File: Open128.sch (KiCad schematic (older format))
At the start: 0 parts

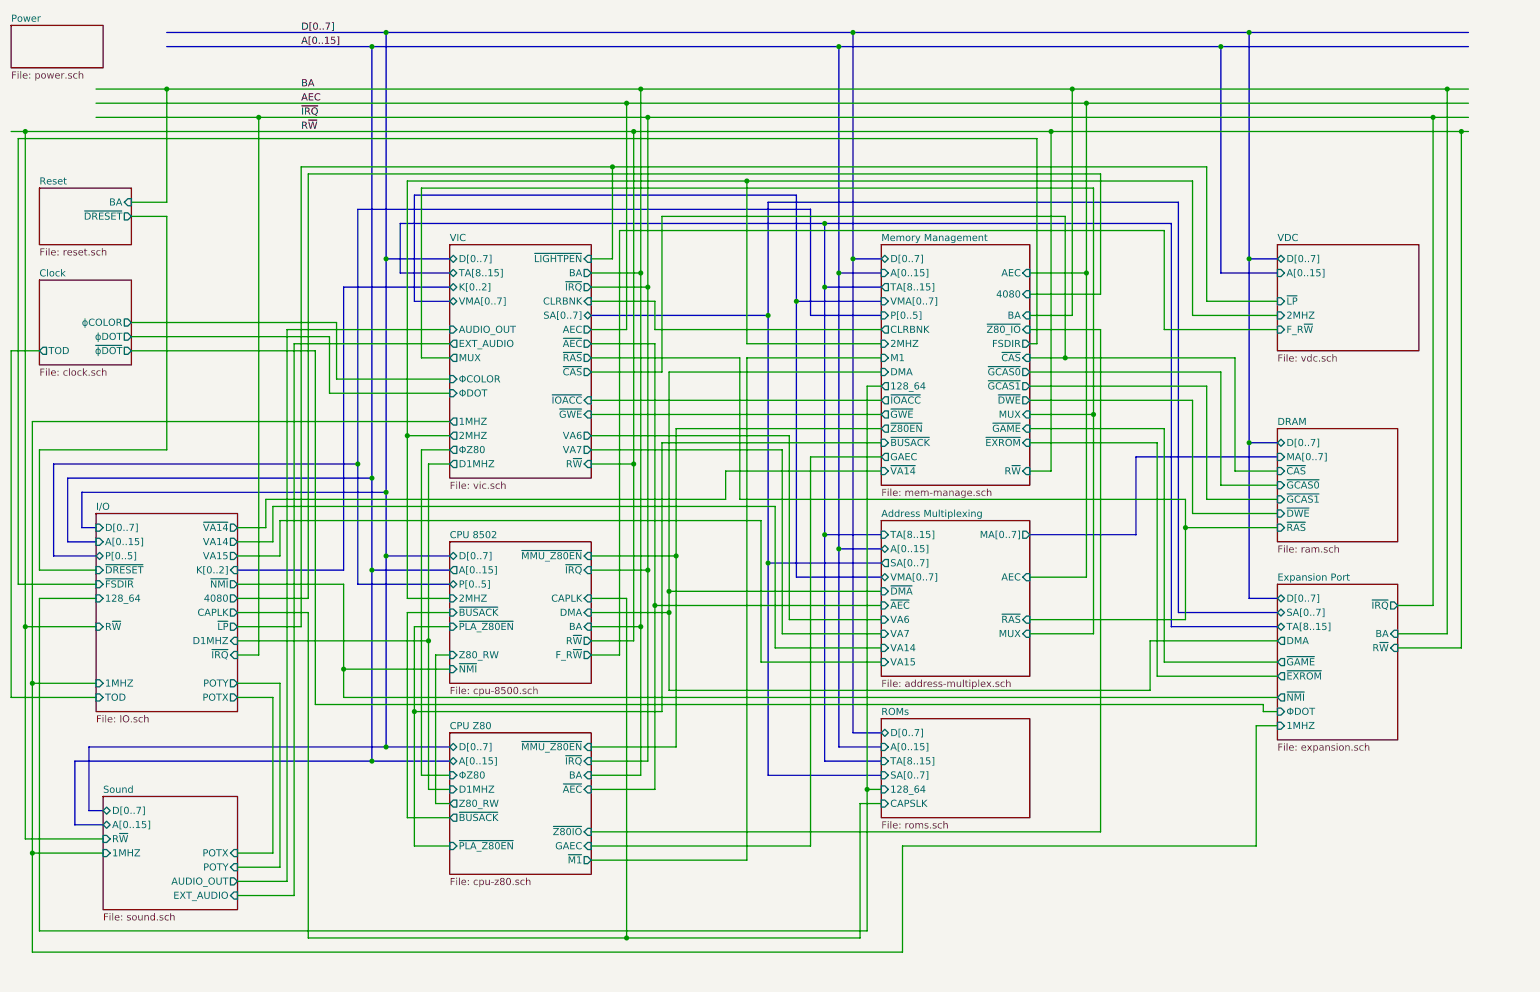
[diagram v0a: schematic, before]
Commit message: Clean up schematic
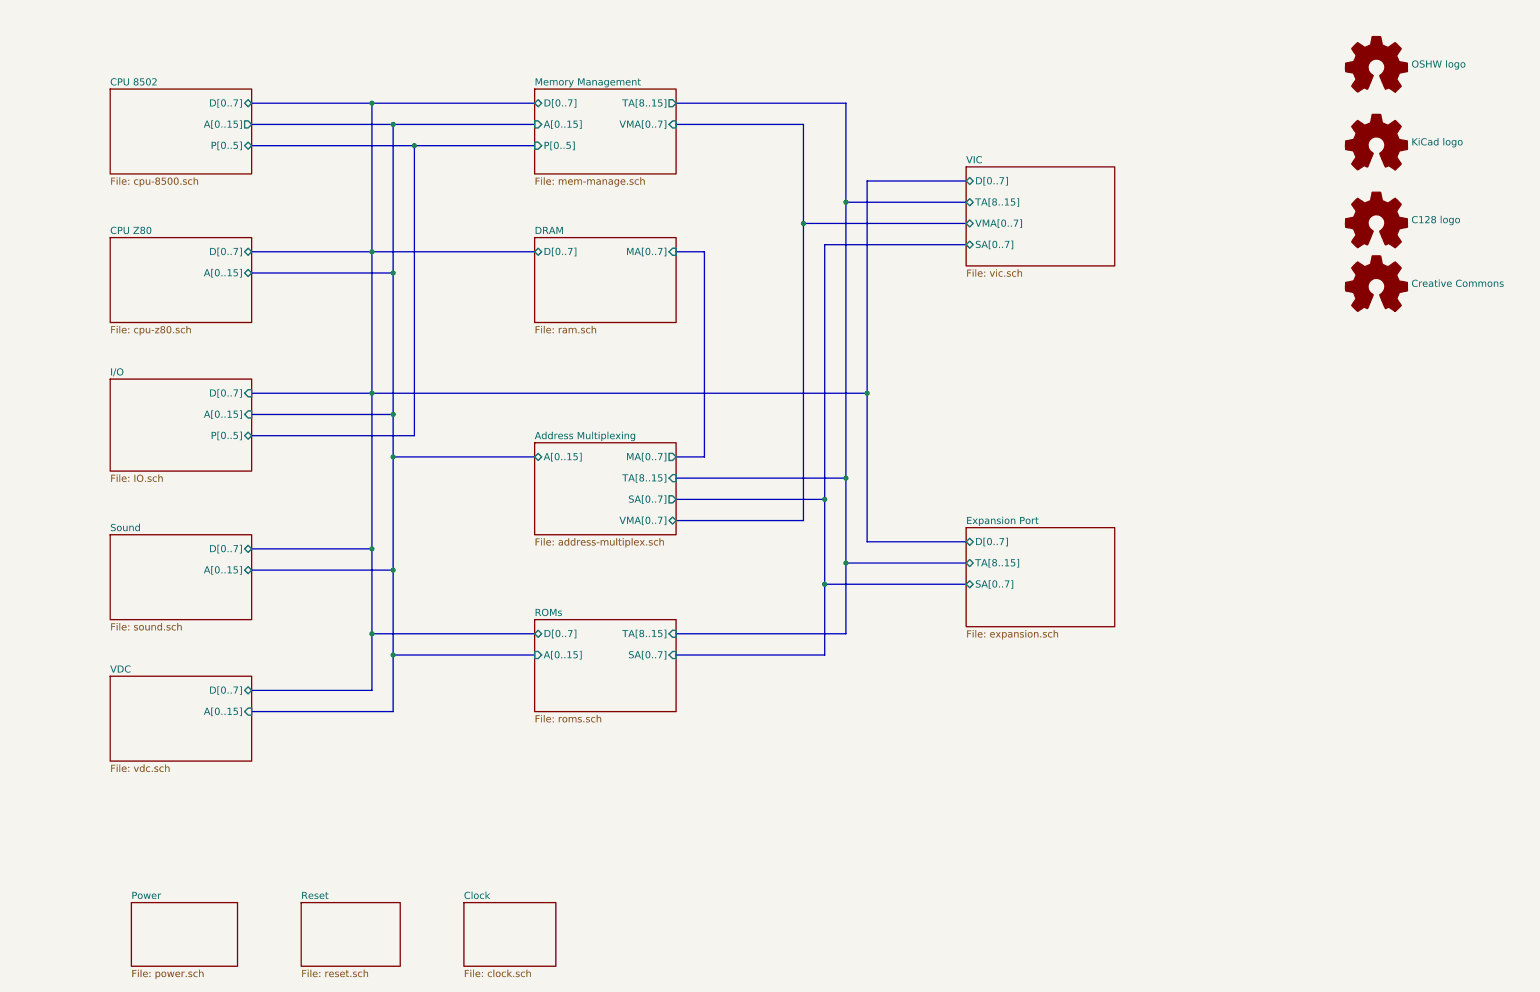
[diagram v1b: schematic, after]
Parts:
- added LOGO1: OSHW logo, Symbol:OSHW-Logo2_48.7x40mm_SilkScreen, symbol Graphic:Logo_Open_Hardware_Small
- added LOGO2: KiCad logo, Symbol:KiCad-Logo2_8mm_SilkScreen, symbol Graphic:Logo_Open_Hardware_Small
- added LOGO3: C128 logo, Open128:C128-logo, symbol Graphic:Logo_Open_Hardware_Small
- added LOGO4: Creative Commons, Symbol:Symbol_CreativeCommons_SilkScreenTop_Type2_Big, symbol Graphic:Logo_Open_Hardware_Small
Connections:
- net labels removed: AEC, A[0..15], BA, D[0..7], R~W, ~IRQ
- wire segments 264 -> 0
